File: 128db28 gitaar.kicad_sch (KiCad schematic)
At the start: 56 parts, among them IC1 L4931CD50-TR, IC2 L4931CD50-TR, J1 NJ2FD-V, J2 NJ2FD-V, J3 Jack-DC, J4 Conn_01x01_Pin, K1 Relay_SPDT, Q1 BC847, U1 TLV9002, U2 TLV9002, U3 APS6404L-3SQRx-SN, U4 AVR128DB28-I_SS, U5 TPS73133DBV

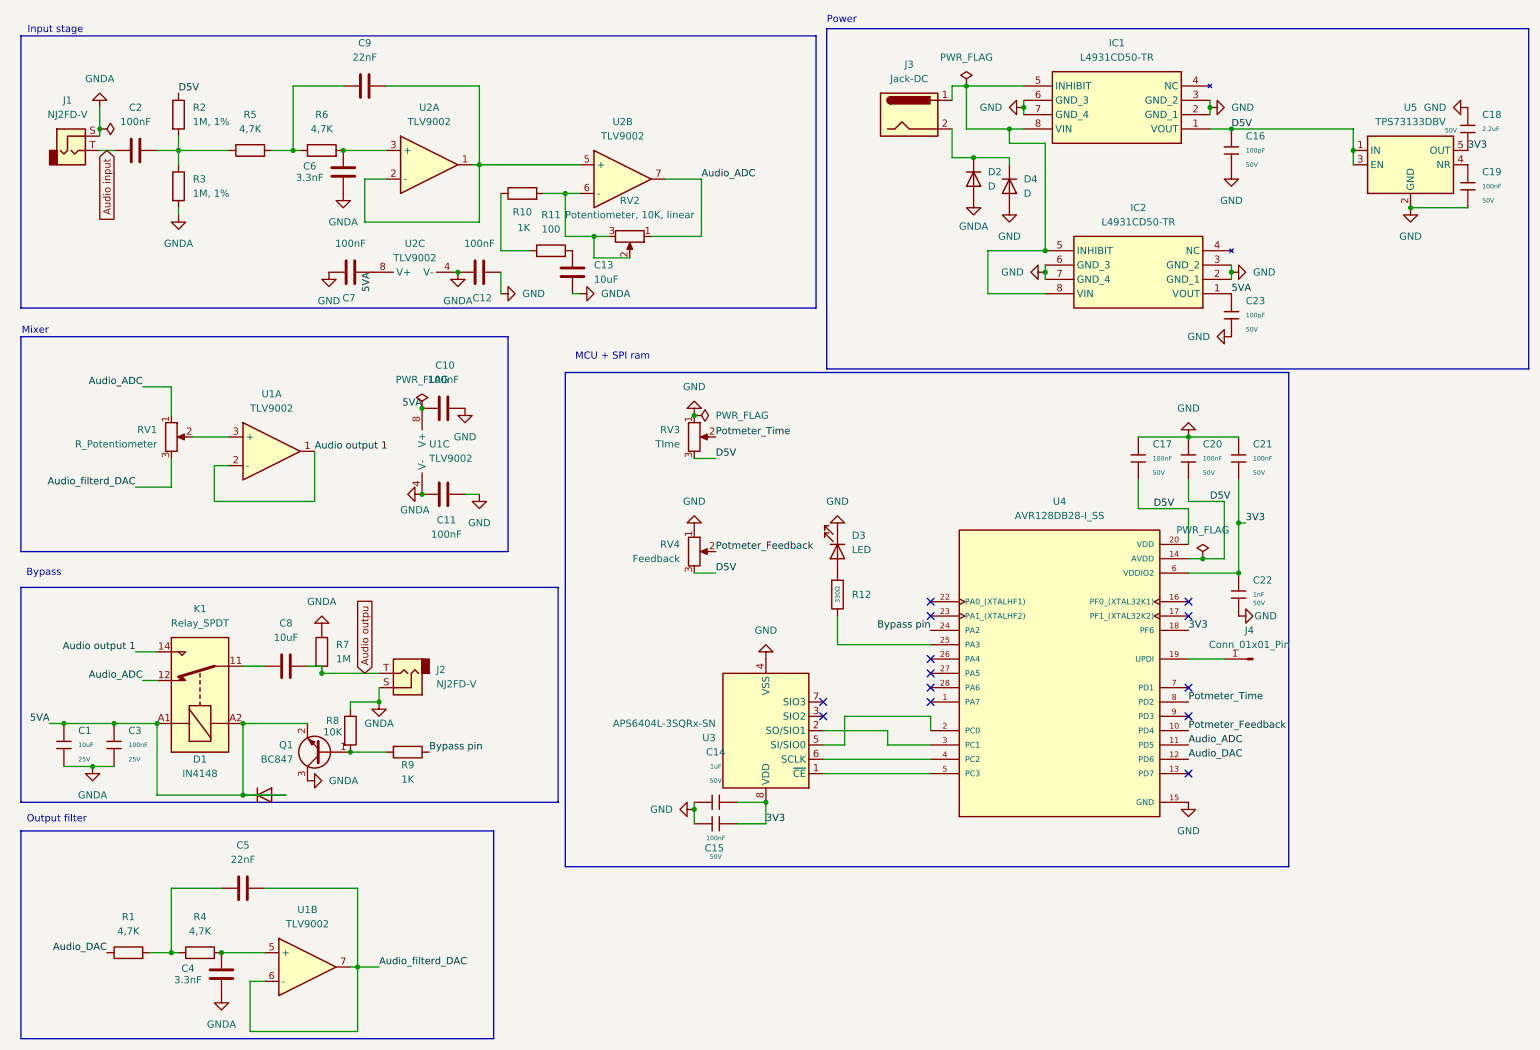
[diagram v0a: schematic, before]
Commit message: added the optocouplers
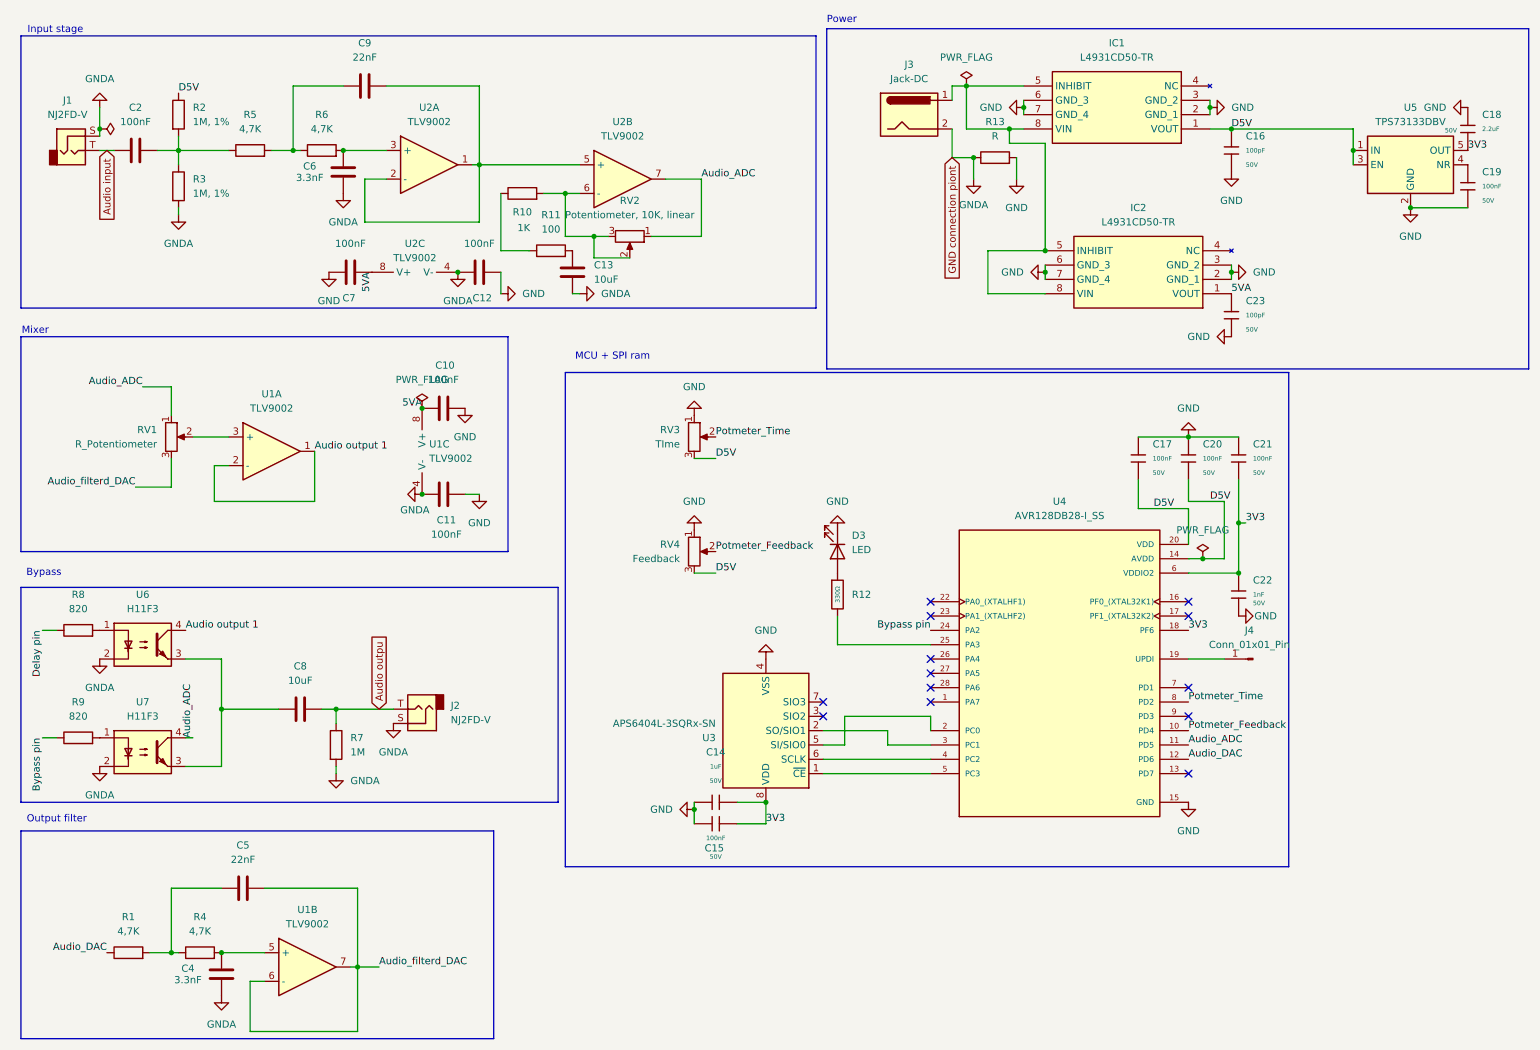
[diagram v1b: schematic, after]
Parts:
- removed C1: 10uF, PCM_JLCPCB:C_1206, symbol V2:1206,10uF
- removed C3: 100nF, PCM_JLCPCB:C_1206, symbol V2:1206,100nF
- removed D1: IN4148, symbol V2:D
- removed D2, D4: D, symbol V2:D
- removed K1: Relay_SPDT, symbol V2:Relay_SPDT
- removed Q1: BC847, Package_TO_SOT_SMD:SOT-23, symbol V2:BC847
- removed R8: 10K, symbol V2:R
- removed R9: 1K, symbol V2:R
- added R13: R, symbol Device:R
- added R8, R9: 820, symbol Device:R
- added U6, U7: H11F3, symbol Isolator:Optocoupler_DC_PhotoNPN_AKEC
- C10, C11, C12, C13, C2, C4, C5, C6, C7, C8, C9: footprint (none) -> PCM_JLCPCB:C_1206
- C15, C16, C17, C18, C19, C20, C21, C22, C23: footprint PCM_JLCPCB:C_0805 -> PCM_JLCPCB:C_1206
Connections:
- net Audio outpu: now also R7.1; no longer R7.2
- net Audio output 1: now also U6.4
- net Audio_ADC: now also U7.4
- net Bypass pin: now also R9.1
- net GND: now also R13.2
- net GNDA: now also J3.2, R7.2, R13.1, U6.2, U7.2; no longer R7.1
- net at C8.1: now also U6.3, U7.3
- new net: R9.2, U7.1
- new net: R8.2, U6.1
- new net Delay pin: R8.1
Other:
- moved on the sheet: C8, J2, R7

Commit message: hopefully this fixe this issue
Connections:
- net Delay pin: now also U4.23 (PA1_(XTALHF2))
- no-connect marks 13 -> 12
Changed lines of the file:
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@@
-	)
-	(no_connect
-		(at 177.8 120.65)
 	)
 	(no_connect
@@
 		)
 	)
+	(label "Delay pin"
+		(at 177.8 120.65 180)
+		(effects
+			(font
+				(size 1.27 1.27)
+			)
+			(justify right bottom)
+		)
+	)

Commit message: fixed some issues i think i am happy now
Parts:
- removed C14: 1uF, Capacitor_SMD:C_1206_3216Metric_Pad1.33x1.80mm_HandSolder, symbol V2:0805,1uF
- removed C15, C17, C19, C20, C21: 100nF, PCM_JLCPCB:C_1206, symbol V2:0805,100nF,(2)
- removed C16, C23: 100pF, PCM_JLCPCB:C_1206, symbol V2:0805,100pF
- removed C18: 2.2uF, PCM_JLCPCB:C_1206, symbol V2:0805,2.2uF
- removed C22: 1nF, PCM_JLCPCB:C_1206, symbol V2:0805,1nF
- removed J1, J2: NJ2FD-V, Connector_Audio:Jack_6.35mm_Neutrik_NJ2FD-V_Vertical, symbol V2:NJ2FD-V
- removed R12: 330Ω, PCM_JLCPCB:R_0805, symbol V2:0805,330Ω
- added C1: 1uF, symbol Device:C
- added C14, C15, C17, C18, C19, C21, C3: 100nF, PCM_JLCPCB:C_1206, symbol Device:C
- added C16: 100pF, PCM_JLCPCB:C_1206, symbol Device:C
- added C20: 1nF, PCM_JLCPCB:C_1206, symbol Device:C
- added J1, J2: 6.3mm TR, symbol Connector:Conn_01x02_Pin
- added R12: 330, PCM_JLCPCB:R_1206, symbol Device:R
- C10, C11, C12, C13, C2, C4, C5, C6, C7, C8, C9: symbol V2:C -> Device:C
- D3: symbol V2:LED -> Device:LED
- J3: symbol V2:Jack-DC -> Connector:Jack-DC
- J4: symbol V2:Conn_01x01_Pin -> Connector:Conn_01x01_Pin
- R1, R10, R11, R2, R3, R4, R5, R6, R7: footprint (none) -> PCM_JLCPCB:R_1206; symbol V2:R -> Device:R
- R13: value R -> 0
- R8, R9: footprint (none) -> PCM_JLCPCB:R_1206
- RV1, RV2, RV3, RV4: symbol V2:R_Potentiometer -> Device:R_Potentiometer
- U1, U2: symbol V2:Opamp_Dual -> Device:Opamp_Dual
- U3: symbol V2:APS6404L-3SQRx-SN -> Memory_RAM:APS6404L-3SQRx-SN
- U4: footprint AVR:SOP65P780X200-28N -> Package_DIP:DIP-28_W7.62mm; symbol V2:AVR128DB28-I_SS -> MCU_Microchip_AVR_Dx:AVR128DB28x-xSP
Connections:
- net 3V3: now also C1.2, C17.1, C18.1, C20.2, C3.2
- net 5VA: now also C21.2
- net Audio input: now also J1.2 (Pin_2)
- net Audio outpu: now also J2.2 (Pin_2)
- net Bypass pin: now also U4.25 (PA3); no longer U4.24 (PA2)
- net D5V: now also C14.1, C15.1, C16.2
- net Delay pin: now also U4.24 (PA2); no longer U4.23 (PA1_(XTALHF2))
- net GND: now also J3.2, C1.1, C14.2, C15.2, C16.1, C17.2, C18.2, C19.1, C20.1, C21.1, C3.1
- net GNDA: now also J1.1 (Pin_1), J2.1 (Pin_1); no longer J3.2
- net at U5.4 (NR): now also C19.2
- net at D3.2 (A): now also R12.1
- net at U3.1 (~{CE}): now also U4.4 (PC2); no longer U4.5 (PC3)
- net at U3.6 (SCLK): now also U4.5 (PC3); no longer U4.4 (PC2)
- net at U4.26 (PA4): now also R12.2
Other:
- moved on the sheet: D3, J4, RV3, RV4, U3
